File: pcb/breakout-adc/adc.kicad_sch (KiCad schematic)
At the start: 89 parts, among them J20 Conn_02x02_Counter_Clockwise, J21 Conn_02x04_Odd_Even, U1 LMH6551MA, U2 LMH6551MA, U3 74AVC9112, U4 ADC10DL065, U5 74LS574, U6 74LS574, U7 74LS574, X1 SG-8101CE 50Mhz

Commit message: [adc][pcb] routed data to buffers
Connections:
- net CLK_FPGA: now also R22.1; no longer R20.1
- net CLK_HDR: now also R20.1; no longer R22.1
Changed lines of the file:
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@@
 	)
 	(label "CLK_HDR"
-		(at 137.16 232.41 0)
+		(at 137.16 229.87 0)
 		(fields_autoplaced yes)
 		(effects
@@
 	)
 	(label "CLK_FPGA"
-		(at 137.16 229.87 0)
-		(fields_autoplaced yes)
-		(effects
+		(at 137.16 232.41 0)
+		(fields_autoplaced yes)
+		(effects

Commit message: [pcb] add FX18-120P footprint and update pcbs
and a few adc fixes, including a key resistor fix
(the op amp for Y had a copy paste error from X
on the positive Rg)
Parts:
- R12: value 2.4k -> 1.8k
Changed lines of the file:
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@@
 			)
 		)
-		(property "Datasheet" "https://www.ti.com/lit/ds/scas301r/scas301r.pdf"
+		(property "Datasheet" "https://www.ti.com/lit/ds/symlink/sn74als574b.pdf"
 			(at 318.77 184.15 0)
 			(effects
@@
 			)
 		)
-		(property "Datasheet" "https://www.ti.com/lit/ds/scas301r/scas301r.pdf"
+		(property "Datasheet" "https://www.ti.com/lit/ds/symlink/sn74als574b.pdf"
 			(at 318.77 127 0)
 			(effects
@@
 			)
 		)
-		(property "Datasheet" "https://www.ti.com/lit/ds/scas301r/scas301r.pdf"
+		(property "Datasheet" "https://www.ti.com/lit/ds/symlink/sn74als574b.pdf"
 			(at 318.77 68.58 0)
 			(effects
@@
 			)
 		)
-		(property "Datasheet" "https://support.epson.biz/td/api/doc_check.php?dl=brief_SG-8101CE"
+		(property "Datasheet" "https://support.epson.biz/td/api/doc_check.php?mode=dl&lang=en&Parts=SG-8 002DC"
 			(at 44.45 241.3 0)
 			(effects
@@
 			)
 		)
-		(property "Value" "2.4k"
+		(property "Value" "1.8k"
 			(at 68.58 149.86 90)
 			(effects

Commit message: [adc][pcb] fully routed
needs some return trace cleanup, return path checks,
gnd/power plane touchups, and some drc fixes/tweaks.
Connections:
- net CLK_FPGA: now also R20.1; no longer R22.1
- net CLK_HDR: now also R22.1; no longer R20.1
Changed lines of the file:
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@@
 	)
 	(label "CLK_HDR"
-		(at 137.16 229.87 0)
+		(at 137.16 232.41 0)
 		(fields_autoplaced yes)
 		(effects
@@
 	)
 	(label "CLK_FPGA"
-		(at 137.16 232.41 0)
-		(fields_autoplaced yes)
-		(effects
+		(at 137.16 229.87 0)
+		(fields_autoplaced yes)
+		(effects

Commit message: [adc][pcb] relink footprints to fix drc issue
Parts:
- U3: footprint VSSOP8_SOT765-1_NEX -> 74AVC9112:VSSOP8_SOT765-1_NEX
- U4: footprint VEC64A_TEX -> ADC10DL065:VEC64A_TEX
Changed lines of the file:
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@@
 		(at 222.25 105.41 0)
 		(unit 1)
-		(exclude_from_sim yes)
+		(exclude_from_sim no)
 		(in_bom yes)
 		(on_board yes)
 		(dnp no)
 		(property "Reference" "U4"
-			(at 221.234 101.854 0)
+			(at 219.71 70.104 0)
 			(effects
 				(font
@@
 		)
 		(property "Value" "ADC10DL065"
-			(at 221.488 104.902 0)
+			(at 219.71 72.644 0)
 			(effects
 				(font
@@
 			)
 		)
-		(property "Footprint" "VEC64A_TEX"
-			(at 222.25 105.41 0)
+		(property "Footprint" "ADC10DL065:VEC64A_TEX"
+			(at 220.218 128.524 0)
 			(effects
 				(font
@@
 		)
 		(property "Datasheet" "https://www.ti.com/lit/ds/symlink/adc10dl065.pdf"
-			(at 222.25 105.41 0)
+			(at 220.98 130.81 0)
 			(effects
 				(font
@@
 		)
 		(property "Description" ""
-			(at 222.25 105.41 0)
+			(at 251.46 146.05 0)
 			(effects
 				(font
@@
 		(at 109.22 228.6 0)
 		(unit 1)
-		(exclude_from_sim yes)
+		(exclude_from_sim no)
 		(in_bom yes)
 		(on_board yes)
 		(dnp no)
 		(property "Reference" "U3"
-			(at 98.044 245.11 0)
+			(at 109.22 216.154 0)
 			(effects
 				(font
@@
 		)
 		(property "Value" "74AVC9112"
-			(at 98.044 247.65 0)
+			(at 109.22 218.694 0)
 			(effects
 				(font
@@
 			)
 		)
-		(property "Footprint" "VSSOP8_SOT765-1_NEX"
-			(at 109.22 228.6 0)
+		(property "Footprint" "74AVC9112:VSSOP8_SOT765-1_NEX"
+			(at 92.456 233.172 0)
 			(effects
 				(font
@@
 		)
 		(property "Datasheet" "74AVC9112DCH"
-			(at 109.22 228.6 0)
+			(at 90.17 233.172 0)
 			(effects
 				(font
@@
 		)
 		(property "Description" ""
-			(at 109.22 228.6 0)
+			(at 96.52 226.06 0)
 			(effects
 				(font

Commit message: [adc][pcb] clear adc simulator flag
also start adding part numbers
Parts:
- C1, C17, C19, C20, C21, C22, C23, C24, C25, C27, C28, C31, C32, C34, C35, C37, C38, C39, C43, C44, C9: Digi-Key Part Number (none) -> 490-6328-1-ND; LCSC Part # (none) -> C1525
- C10, C2, C26, C29, C30, C33, C36: Digi-Key Part Number (none) -> 490-3896-1-ND; LCSC Part # (none) -> C77041
- C11, C12, C3, C4: Digi-Key Part Number (none) -> 490-6328-1-ND; LCSC Part # (none) -> C71629
- C13, C16, C5, C8: Digi-Key Part Number (none) -> 490-3247-1-ND; LCSC Part # (none) -> C437449
- C14, C15, C6, C7: Digi-Key Part Number (none) -> 490-GRT1555C1H161FA02DCT-ND; LCSC Part # (none) -> C2188753

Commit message: [adc][pcb] add remaining part numbers
missing test points for lcsc, but otherwise done
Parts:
- J20: Digi-Key Part Number (none) -> 952-2119-ND
- J21: Digi-Key Part Number (none) -> 952-2122-ND
- R10, R11, R13, R14, R17, R4, R6, R7: Digi-Key Part Number (none) -> YAG1606CT-ND; LCSC Part # (none) -> C861270
- R12: value 1.8k -> 1.82k; Digi-Key Part Number (none) -> YAG1575CT-ND; LCSC Part # (none) -> C705745
- R15, R16: value 900 -> 910; Digi-Key Part Number (none) -> YAG1748CT-ND; LCSC Part # (none) -> C861598
- R18, R19, R20, R22, R23: Digi-Key Part Number (none) -> 311-22.0HRCT-ND; LCSC Part # (none) -> C107701
- R21: Digi-Key Part Number (none) -> 311-1.00KHRCT-ND; LCSC Part # (none) -> C22548
- R24: footprint Resistor_SMD:R_0402_1005Metric -> Resistor_SMD:R_0603_1608Metric; Digi-Key Part Number (none) -> 311-1.00KHRCT-ND; LCSC Part # (none) -> C22548
- R45, R46: Digi-Key Part Number (none) -> 311-10.0KHRCT-ND; LCSC Part # (none) -> C98220
- R5: Digi-Key Part Number (none) -> YAG1619CT-ND; LCSC Part # (none) -> C861300
- R8, R9: Digi-Key Part Number (none) -> YAG1563CT-ND; LCSC Part # (none) -> C136970
- U1, U2: Digi-Key Part Number (none) -> LMH6551MA/NOPB-ND; LCSC Part # (none) -> C529311
- U3: Digi-Key Part Number (none) -> 1727-7845-1-ND; LCSC Part # (none) -> C546283
- U4: Digi-Key Part Number (none) -> ADC10DL065CIVS/NOPB-ND; LCSC Part # (none) -> C2877193

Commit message: [adc][pcb] fix digikey part num for 0.01uf cap
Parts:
- C11, C12, C3, C4: Digi-Key Part Number 490-6328-1-ND -> 490-3261-1-ND
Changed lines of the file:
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@@
 			)
 		)
-		(property "Digi-Key Part Number" "490-6328-1-ND"
+		(property "Digi-Key Part Number" "490-3261-1-ND"
 			(at 107.95 38.1 0)
 			(effects
@@
 			)
 		)
-		(property "Digi-Key Part Number" "490-6328-1-ND"
+		(property "Digi-Key Part Number" "490-3261-1-ND"
 			(at 95.25 38.1 0)
 			(effects
@@
 			)
 		)
-		(property "Digi-Key Part Number" "490-6328-1-ND"
+		(property "Digi-Key Part Number" "490-3261-1-ND"
 			(at 107.95 124.46 0)
 			(effects
@@
 			)
 		)
-		(property "Digi-Key Part Number" "490-6328-1-ND"
+		(property "Digi-Key Part Number" "490-3261-1-ND"
 			(at 95.25 124.46 0)
 			(effects

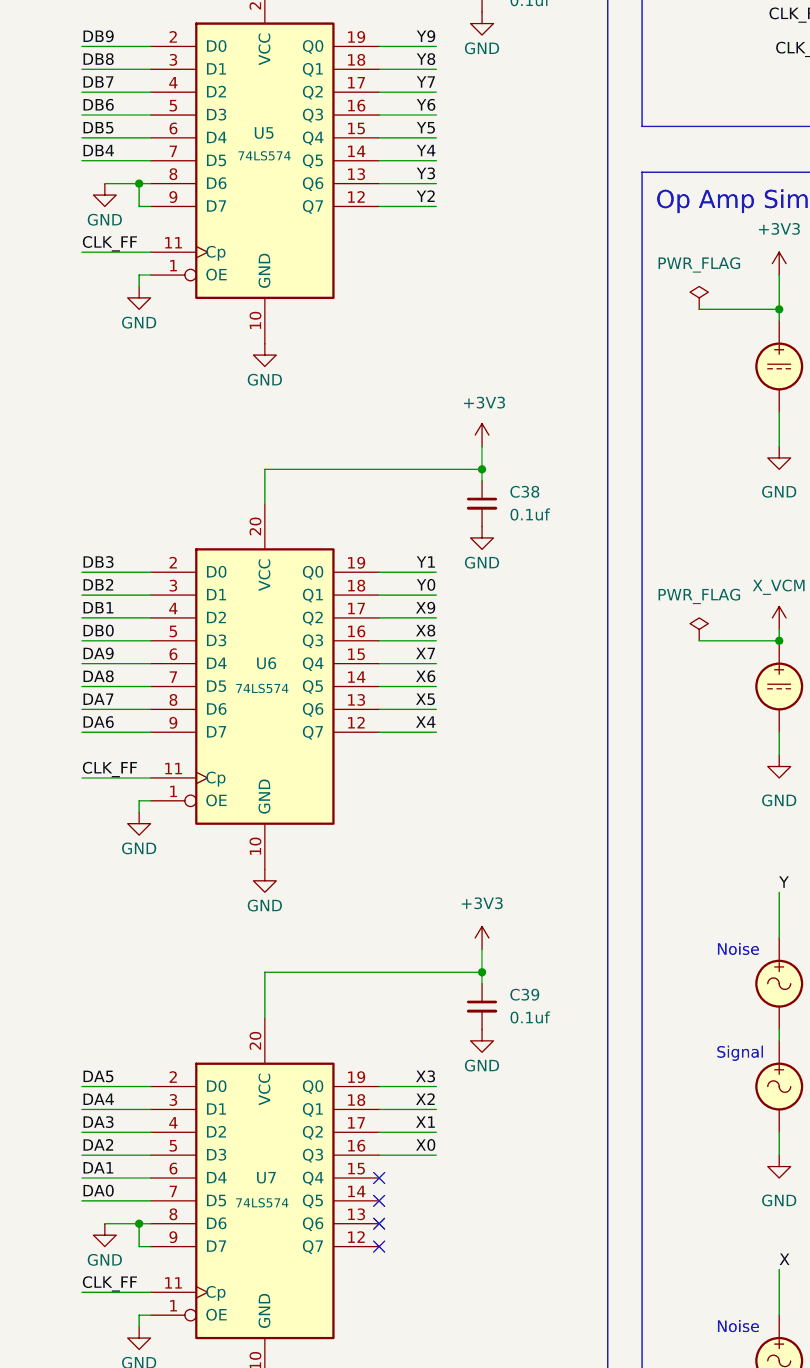
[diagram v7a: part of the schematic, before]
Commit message: [adc][pcb] fix output buffer schematic and routing
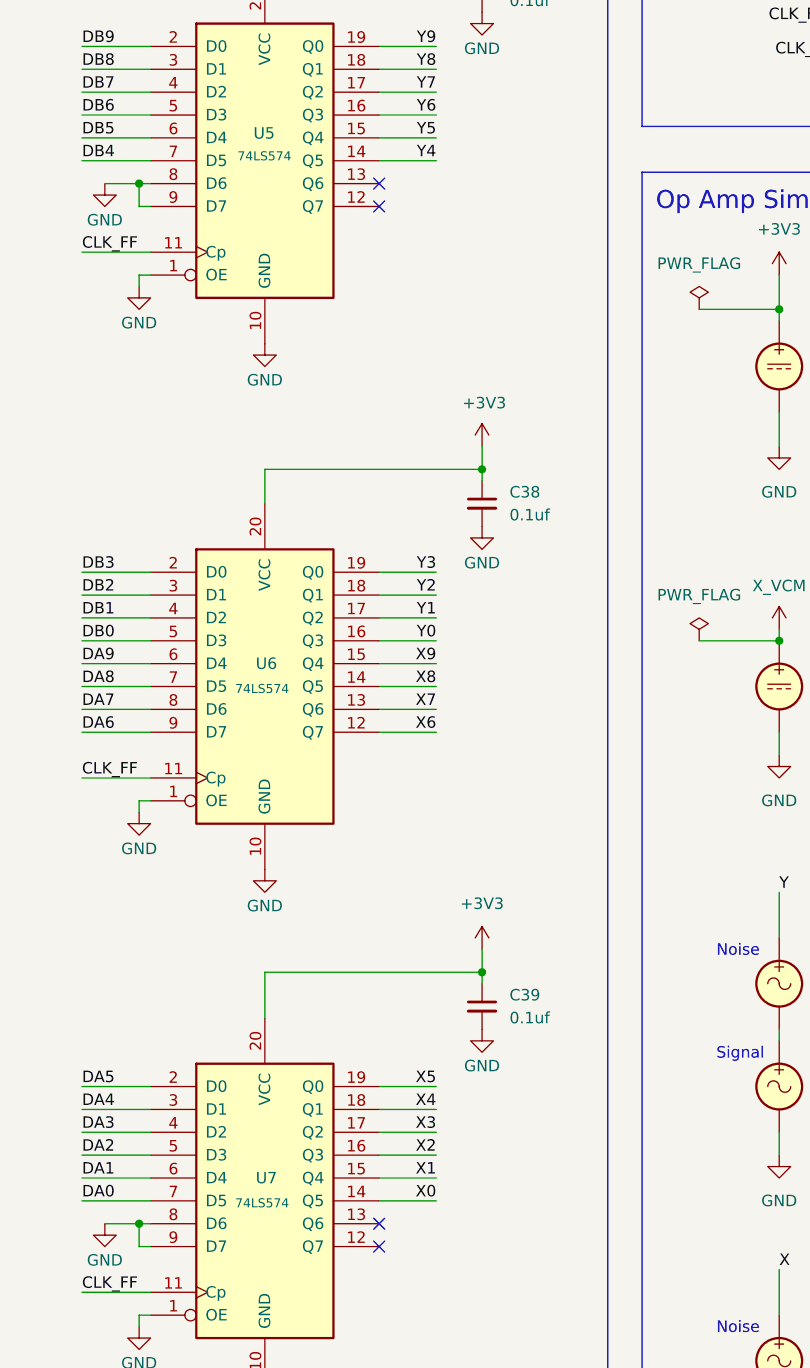
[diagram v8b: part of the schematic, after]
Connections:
- net X0: now also U7.14 (Q5); no longer U7.16 (Q3)
- net X1: now also U7.15 (Q4); no longer U7.17 (Q2)
- net X2: now also U7.16 (Q3); no longer U7.18 (Q1)
- net X3: now also U7.17 (Q2); no longer U7.19 (Q0)
- net X4: now also U7.18 (Q1); no longer U6.12 (Q7)
- net X5: now also U7.19 (Q0); no longer U6.13 (Q6)
- net X6: now also U6.12 (Q7); no longer U6.14 (Q5)
- net X7: now also U6.13 (Q6); no longer U6.15 (Q4)
- net X8: now also U6.14 (Q5); no longer U6.16 (Q3)
- net X9: now also U6.15 (Q4); no longer U6.17 (Q2)
- net Y0: now also U6.16 (Q3); no longer U6.18 (Q1)
- net Y1: now also U6.17 (Q2); no longer U6.19 (Q0)
- net Y2: now also U6.18 (Q1); no longer U5.12 (Q7)
- net Y3: now also U6.19 (Q0); no longer U5.13 (Q6)
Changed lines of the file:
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@@
 	)
 	(no_connect
-		(at 331.47 181.61)
+		(at 331.47 73.66)
 	)
 	(no_connect
-		(at 177.8 175.26)
+		(at 331.47 71.12)
 	)
 	(no_connect
-		(at 331.47 184.15)
+		(at 177.8 175.26)
 	)
 	(no_connect
@@
 	(wire
 		(pts
+			(xy 331.47 181.61) (xy 337.82 181.61)
+		)
+		(stroke
+			(width 0)
+			(type default)
+		)
+	)
+	(wire
+		(pts
 			(xy 76.2 142.24) (xy 99.06 142.24)
 		)
@@
 	(wire
 		(pts
+			(xy 331.47 184.15) (xy 337.82 184.15)
+		)
+		(stroke
+			(width 0)
+			(type default)
+		)
+	)
+	(wire
+		(pts
 			(xy 265.43 80.01) (xy 271.78 80.01)
 		)
@@
 	(wire
 		(pts
-			(xy 331.47 73.66) (xy 337.82 73.66)
-		)
-		(stroke
-			(width 0)
-			(type default)
-		)
-	)
-	(wire
-		(pts
 			(xy 87.63 166.37) (xy 87.63 167.64)
 		)
@@
 	(wire
 		(pts
-			(xy 331.47 71.12) (xy 337.82 71.12)
-		)
-		(stroke
-			(width 0)
-			(type default)
-		)
-	)
-	(wire
-		(pts
 			(xy 45.72 78.74) (xy 57.15 78.74)
 		)
@@
 	)
 	(label "X3"
-		(at 337.82 171.45 180)
+		(at 337.82 176.53 180)
 		(fields_autoplaced yes)
 		(effects
@@
 	)
 	(label "X7"
-		(at 337.82 124.46 180)
+		(at 337.82 129.54 180)
 		(fields_autoplaced yes)
 		(effects
@@
 	)
 	(label "X4"
-		(at 337.82 132.08 180)
+		(at 337.82 173.99 180)
 		(fields_autoplaced yes)
 		(effects
@@
 	)
 	(label "X2"
-		(at 337.82 173.99 180)
+		(at 337.82 179.07 180)
 		(fields_autoplaced yes)
 		(effects
@@
 	)
 	(label "X8"
-		(at 337.82 121.92 180)
+		(at 337.82 127 180)
 		(fields_autoplaced yes)
 		(effects
@@
 	)
 	(label "X0"
-		(at 337.82 179.07 180)
+		(at 337.82 184.15 180)
 		(fields_autoplaced yes)
 		(effects
@@
 	)
 	(label "X5"
-		(at 337.82 129.54 180)
+		(at 337.82 171.45 180)
 		(fields_autoplaced yes)
 		(effects
@@
 	)
 	(label "Y1"
-		(at 337.82 114.3 180)
+		(at 337.82 119.38 180)
 		(fields_autoplaced yes)
 		(effects
@@
 	)
 	(label "Y0"
-		(at 337.82 116.84 180)
+		(at 337.82 121.92 180)
 		(fields_autoplaced yes)
 		(effects
@@
 	)
 	(label "X6"
-		(at 337.82 127 180)
+		(at 337.82 132.08 180)
 		(fields_autoplaced yes)
 		(effects
@@
 	)
 	(label "Y3"
-		(at 337.82 71.12 180)
+		(at 337.82 114.3 180)
 		(fields_autoplaced yes)
 		(effects
@@
 	)
 	(label "X1"
-		(at 337.82 176.53 180)
+		(at 337.82 181.61 180)
 		(fields_autoplaced yes)
 		(effects
@@
 	)
 	(label "X9"
-		(at 337.82 119.38 180)
+		(at 337.82 124.46 180)
 		(fields_autoplaced yes)
 		(effects
@@
 	)
 	(label "Y2"
-		(at 337.82 73.66 180)
+		(at 337.82 116.84 180)
 		(fields_autoplaced yes)
 		(effects
